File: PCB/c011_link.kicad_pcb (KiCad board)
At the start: 2 copper layers, 92.7 x 71.1 mm, 8 parts, among them J1 Conn_02x20_Odd_Even, J2 Conn_01x07, U1 C011, U2 TXS0108EPW_DIP20, U3 TXS0108EPW_DIP20, X1 CXO_DIP14

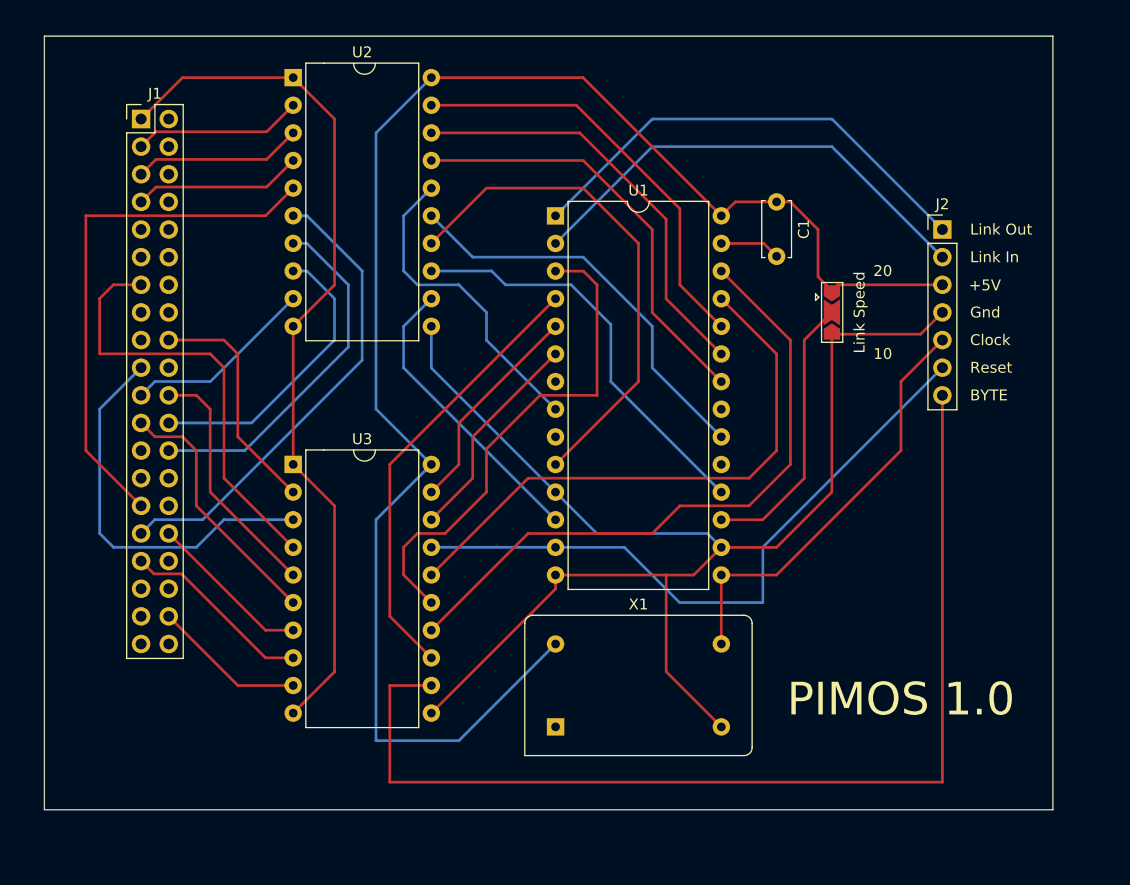
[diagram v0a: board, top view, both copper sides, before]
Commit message: Update to PCB 1.1 design
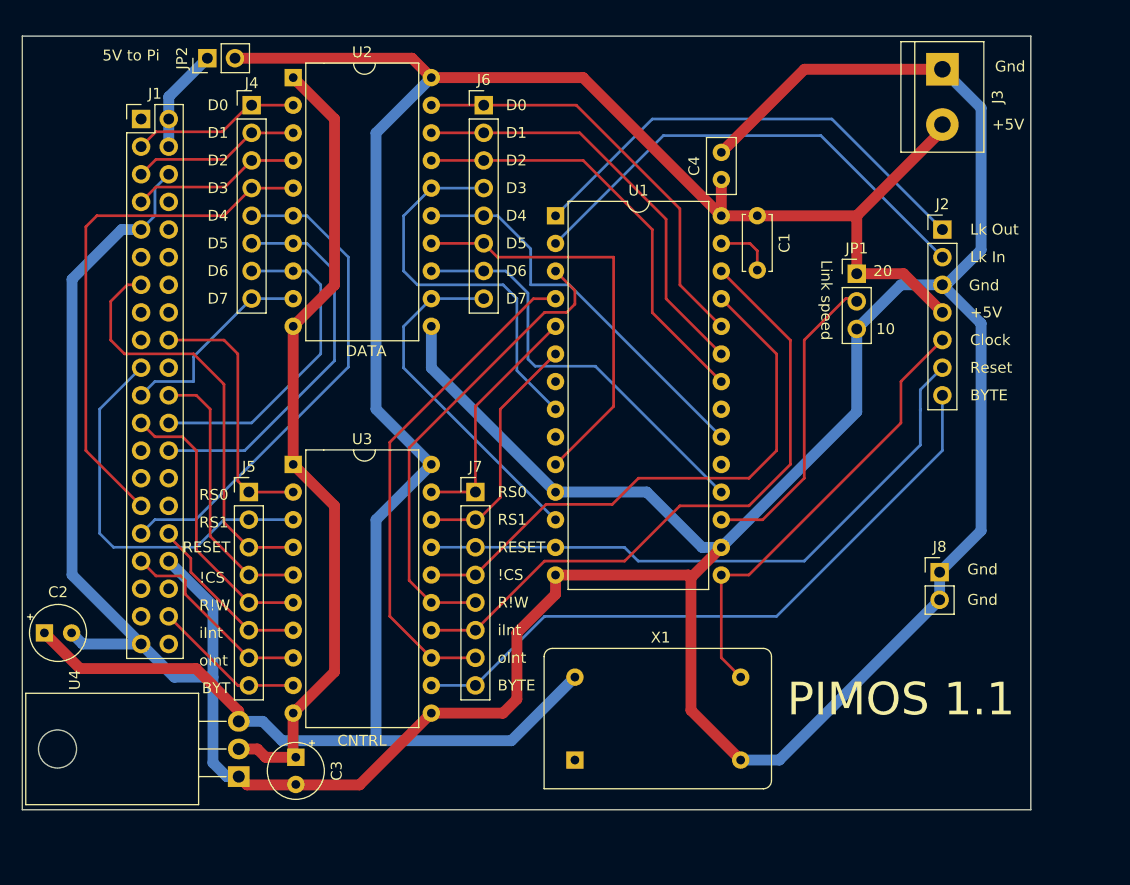
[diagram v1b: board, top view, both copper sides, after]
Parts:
- removed Link Speed: SolderJumper_3_Open, Jumper:SolderJumper-3_P2.0mm_Open_TrianglePad1.0x1.5mm
- added C2: 10uF, Capacitor_THT:CP_Radial_Tantal_D5.0mm_P2.50mm, F.Cu at (67.3, 82.8)
- added C3: 10uF, Capacitor_THT:CP_Radial_Tantal_D5.0mm_P2.50mm, F.Cu at (90.4, 94.2)
- added C4: 100nF, Capacitor_THT:C_Disc_D5.0mm_W2.5mm_P2.50mm, F.Cu at (129.5, 41.1)
- added J3: Power, TerminalBlock:TerminalBlock_bornier-2_P5.08mm, F.Cu at (149.9, 31.0)
- added J4: Debug data 3V3, Connector_PinHeader_2.54mm:PinHeader_1x08_P2.54mm_Vertical, F.Cu at (86.4, 34.3)
- added J5: Debug control 3V3, Connector_PinHeader_2.54mm:PinHeader_1x08_P2.54mm_Vertical, F.Cu at (86.1, 69.8)
- added J6: Debug data 5V, Connector_PinHeader_2.54mm:PinHeader_1x08_P2.54mm_Vertical, F.Cu at (107.7, 34.3)
- added J7: Debug control 5V, Connector_PinHeader_2.54mm:PinHeader_1x08_P2.54mm_Vertical, F.Cu at (106.9, 69.8)
- added J8: Gnd, Connector_PinHeader_2.54mm:PinHeader_1x02_P2.54mm_Vertical, F.Cu at (149.6, 77.2)
- added JP1: Link speed, Connector_PinHeader_2.54mm:PinHeader_1x03_P2.54mm_Vertical, F.Cu at (142.0, 49.8)
- added JP2: 5V to Pi, Connector_PinHeader_2.54mm:PinHeader_1x02_P2.54mm_Vertical, F.Cu at (82.3, 30.0)
- added U4: LT1086-3.3, Package_TO_SOT_THT:TO-220-3_Horizontal_TabDown, F.Cu at (85.2, 96.0)
- C1: value C (0.1uF) -> 0.1uF
- J1: value Conn_02x20_Odd_Even -> RPi
- moved X1 3.53 mm to (116.1, 94.5)
- moved C1 2.18 mm to (132.8, 44.5)
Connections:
- J1 pad 1: +3V3 -> unconnected-(J1-Pad1)
- J1 pad 2: unconnected-(J1-Pad2) -> Net-(J1-Pad4)
- J1 pad 34: unconnected-(J1-Pad34) -> GND
- J1 pad 39: unconnected-(J1-Pad39) -> GND
- J1 pad 4: unconnected-(J1-Pad4) -> Net-(J1-Pad4)
- J1 pad 6: unconnected-(J1-Pad6) -> GND
- J1 pad 9: unconnected-(J1-Pad9) -> GND
- J2 pad 3: +5V -> GND
- J2 pad 4: GND -> +5V
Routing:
- net GND: track 124.8 -> 339.9 mm
- net +5V: track 146.4 -> 215.9 mm
- net HByte: track 99.1 -> 61.0 mm
- net Net-(J1-Pad4): track 0.00 -> 9.60 mm
- net HD5: track 46.7 -> 38.5 mm
- net HD3: track 29.4 -> 36.6 mm
- net +3V3: track 80.3 -> 74.1 mm
- net HOutputInt: track 40.9 -> 46.2 mm
- net HD7: track 27.2 -> 32.0 mm
- net HReset: track 61.0 -> 58.0 mm
- net HRnotW: track 46.5 -> 43.6 mm
- net Net-(U1-Pad17): track 25.5 -> 28.3 mm
- net LD5: track 32.8 -> 35.6 mm
- net LD6: track 27.1 -> 29.8 mm
- net HRS1: track 20.0 -> 22.5 mm
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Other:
- board text added: "!CS"
- board text added: "5V to Pi"
- board text added: "BYT"
- board text added: "CNTRL"
- board text added: "D0"
- board text added: "D1"
- board text added: "D2"
- board text added: "D3"
- board text added: "D4"
- board text added: "D5"
- board text added: "D6"
- board text added: "D7"
- board text added: "DATA"
- board text added: "Link speed"
- board text added: "Lk In"
- board text added: "Lk Out"
- board text added: "PIMOS 1.1"
- board text added: "R!W"
- board text added: "RESET"
- board text added: "RS0"
- board text added: "RS1"
- board text added: "iInt"
- board text added: "oInt"
- board text removed: "Link In"
- board text removed: "Link Out"
- board text removed: "PIMOS 1.0"

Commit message: move to 74LVC8T245 level converters
The existing auto detecting direction shifters can glitch into the 'wrong' direction
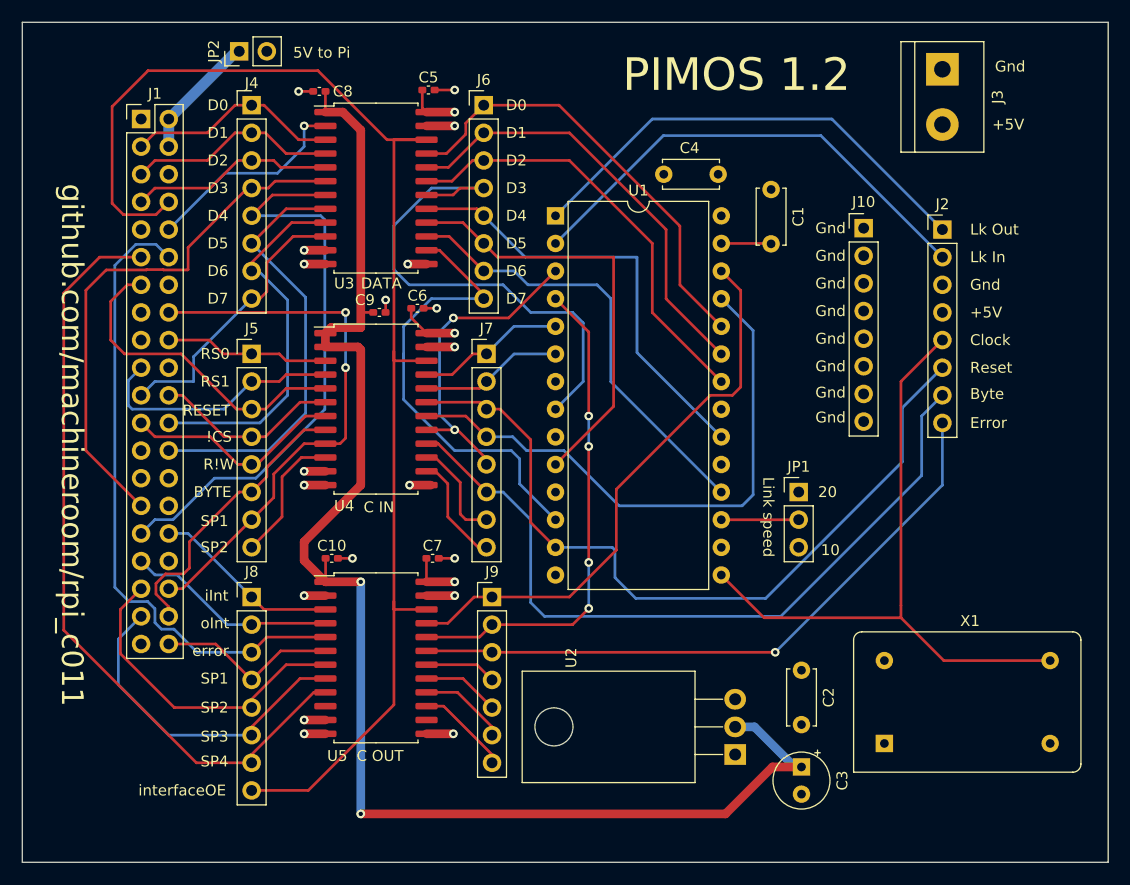
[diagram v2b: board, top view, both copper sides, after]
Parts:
- removed the U2 at (90.2, 31.8)
- added C10: 0.1uF, Capacitor_SMD:C_0402_1005Metric_Pad0.74x0.62mm_HandSolder, F.Cu at (93.7, 75.9)
- added C5: 0.1uF, Capacitor_SMD:C_0402_1005Metric_Pad0.74x0.62mm_HandSolder, F.Cu at (102.6, 32.9)
- added C6: 0.1uF, Capacitor_SMD:C_0402_1005Metric_Pad0.74x0.62mm_HandSolder, F.Cu at (101.6, 53.0)
- added C7: 0.1uF, Capacitor_SMD:C_0402_1005Metric_Pad0.74x0.62mm_HandSolder, F.Cu at (103.0, 75.9)
- added C8: 0.1uF, Capacitor_SMD:C_0402_1005Metric_Pad0.74x0.62mm_HandSolder, F.Cu at (92.6, 33.0)
- added C9: 0.1uF, Capacitor_SMD:C_0402_1005Metric_Pad0.74x0.62mm_HandSolder, F.Cu at (98.1, 53.3)
- added J8: Debug control out 3V3, Connector_PinHeader_2.54mm:PinHeader_1x08_P2.54mm_Vertical, F.Cu at (86.4, 79.5)
- added J9: Debug control out 5V, Connector_PinHeader_2.54mm:PinHeader_1x07_P2.54mm_Vertical, F.Cu at (108.5, 79.5)
- added U4: 74LVC8T245, Package_SO:SOIC-24W_7.5x15.4mm_P1.27mm, F.Cu at (97.8, 62.2)
- added U5: 74LVC8T245, Package_SO:SOIC-24W_7.5x15.4mm_P1.27mm, F.Cu at (97.8, 85.1)
- C2: value 10uF -> 0.1uF; footprint Capacitor_THT:CP_Radial_Tantal_D5.0mm_P2.50mm -> Capacitor_THT:C_Disc_D5.0mm_W2.5mm_P5.00mm
- C4: footprint Capacitor_THT:C_Disc_D5.0mm_W2.5mm_P2.50mm -> Capacitor_THT:C_Disc_D5.0mm_W2.5mm_P5.00mm
- J10: renamed from J8; footprint Connector_PinHeader_2.54mm:PinHeader_1x02_P2.54mm_Vertical -> Connector_PinHeader_2.54mm:PinHeader_1x08_P2.54mm_Vertical
- J2: value Conn_01x07 -> Transputer interface; footprint Connector_PinHeader_2.54mm:PinHeader_1x07_P2.54mm_Vertical -> Connector_PinHeader_2.54mm:PinHeader_1x08_P2.54mm_Vertical
- J5: value Debug control 3V3 -> Debug control in 3V3
- J7: value Debug control 5V -> Debug control in 5V
- U3: value TXS0108EPW_DIP20 -> 74LVC8T245; footprint Package_DIP:DIP-20_W12.7mm -> Package_SO:SOIC-24W_7.5x15.4mm_P1.27mm
- moved C2 69.7 mm to (136.9, 86.2), turned to -90 degrees
- moved C3 46.5 mm to (136.9, 95.1)
- moved U2 45.7 mm to (130.8, 94.0)
- moved J10 32.4 mm to (142.6, 45.6)
- moved X1 28.5 mm to (144.5, 93.0)
- moved U3 26.5 mm to (97.8, 41.9)
- moved JP1 20.8 mm to (136.7, 69.8)
- moved J7 12.7 mm to (108.0, 57.1)
- moved J5 12.7 mm to (86.4, 57.1)
- moved JP2 2.99 mm to (85.2, 29.3)
- moved C1 2.73 mm to (134.1, 42.0)
- moved C4 0.57 mm to (129.2, 40.6), turned to 180 degrees
- renumbered U4 to U2
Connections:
- J1 pad 10: unconnected-(J1-Pad10) -> LByteDir
- J1 pad 11: unconnected-(J1-Pad11) -> LOutSpare4
- J1 pad 12: unconnected-(J1-Pad12) -> LError
- J1 pad 14: unconnected-(J1-Pad14) -> GND
- J1 pad 16: unconnected-(J1-Pad16) -> LInSpare1
- J1 pad 20: unconnected-(J1-Pad20) -> GND
- J1 pad 25: unconnected-(J1-Pad25) -> GND
- J1 pad 30: unconnected-(J1-Pad30) -> GND
- J1 pad 35: unconnected-(J1-Pad35) -> LOutSpare2
- J1 pad 36: unconnected-(J1-Pad36) -> LInSpare1
- J1 pad 37: unconnected-(J1-Pad37) -> LOutSpare3
- J1 pad 40: unconnected-(J1-Pad40) -> LOutSpare1
- J1 pad 8: unconnected-(J1-Pad8) -> LInterfaceOE
- J5 pad 6: LInputInt -> LByte
- J5 pad 7: LOutputInt -> LInSpare1
- J5 pad 8: LByte -> LInSpare2
- J7 pad 6: HInputInt -> HByte
- J7 pad 7: HOutputInt -> HInSpare1
- J7 pad 8: HByte -> HInSpare2
- U3 pad 10: +3V3 -> LD7
- U3 pad 12: HByte -> GND
- U3 pad 13: HOutputInt -> GND
- U3 pad 14: HInputInt -> HD7
- U3 pad 15: HRnotW -> HD6
- U3 pad 16: HnotCS -> HD5
- U3 pad 17: HReset -> HD4
- U3 pad 18: HRS1 -> HD3
- U3 pad 19: HRS0 -> HD2
- U3 pad 2: LRS0 -> LByteDir
- U3 pad 20: +5V -> HD1
- U3 pad 3: LRS1 -> LD0
- U3 pad 4: LReset -> LD1
- U3 pad 5: LnotCS -> LD2
- U3 pad 6: LRnotW -> LD3
- U3 pad 7: LInputInt -> LD4
- U3 pad 8: LOutputInt -> LD5
- U3 pad 9: LByte -> LD6
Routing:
- net GND: track 339.9 -> 28.1 mm, vias 0 -> 16
- net +5V: track 215.9 -> 22.8 mm, vias 0 -> 6
- net LInterfaceOE: track 0.00 -> 126.9 mm
- net LOutSpare4: track 0.00 -> 71.7 mm
- net +3V3: track 74.1 -> 135.5 mm, vias 0 -> 2
- net HError: track 0.00 -> 59.6 mm, vias 0 -> 1
- net LError: track 0.00 -> 59.0 mm
- net LInSpare1: track 0.00 -> 51.1 mm, vias 0 -> 2
- net LOutSpare3: track 0.00 -> 30.7 mm
- net LOutSpare2: track 0.00 -> 29.7 mm
- net Net-(JP1-Pad2): track 28.3 -> 7.12 mm
- net LByteDir: track 0.00 -> 19.5 mm, vias 0 -> 1
- net CLK: track 41.6 -> 60.6 mm
- net LOutSpare1: track 0.00 -> 16.9 mm
- net HReset: track 58.0 -> 72.5 mm
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- added copper zone on In1.Cu, net +5V
- added copper zone on In2.Cu, net GND
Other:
- board size 92.7 x 71.1 mm -> 99.8 x 77.2 mm
- copper layers 2 -> 4
- board text added: "Byte"
- board text added: "C IN"
- board text added: "C OUT"
- board text added: "Error"
- board text added: "PIMOS 1.2"
- board text added: "SP1"
- board text added: "SP2"
- board text added: "SP3"
- board text added: "SP4"
- board text added: "error"
- board text added: "github.com/machineroom/rpi_c011"
- board text added: "interfaceOE"
- board text removed: "BYT"
- board text removed: "CNTRL"
- board text removed: "PIMOS 1.1"
